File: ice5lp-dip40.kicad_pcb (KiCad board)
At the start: 4 copper layers, 17.8 x 50.8 mm, 44 parts, among them J1 Conn_02x04_Odd_Even, J2 Conn_01x20, J3 Conn_01x20, J4 USB_B_Micro, SW1 SW_Push, SW2 SW_Push, U1 AT25D011-SSHF, U2 MIC5355-S4YMME, U3 ICE5LP4K-SG48, X1 ECS-2520MV-500-BN-TR

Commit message: Archive project 3d models
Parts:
- C1, C10, C11, C12, C13, C15, C17, C18, C19, C2, C20, C3, C4, C7, C8, C9: footprint esynr3z_Capacitor:C_0603 -> lib_fp:C_0603
- D1: footprint esynr3z_Diode:SOD-523F -> lib_fp:SOD-523F
- D2: footprint esynr3z_LED:LED_Cree-PLCC4_2x2mm_CW -> lib_fp:LED_Cree-PLCC4_2x2mm_CW
- D3, D4, D5: footprint esynr3z_LED:LED_0603 -> lib_fp:LED_0603
- J1: footprint esynr3z_Connector:PinHeader_2x04_P2.54mm_Vertical -> lib_fp:PinHeader_2x04_P2.54mm_Vertical
- J2, J3: footprint esynr3z_Connector:PinHeader_1x20_P2.54mm_Vertical -> lib_fp:PinHeader_1x20_P2.54mm_Vertical
- J4: footprint esynr3z_ConnectorUSB:USB_Micro-B_Wurth_629105136821 -> lib_fp:USB_Micro-B_Wurth_629105136821
- R1, R10, R11, R12, R13, R2, R4, R5, R6, R7, R8, R9: footprint esynr3z_Resistor:R_0603 -> lib_fp:R_0603
- SW1, SW2: footprint esynr3z_Switch:PTS830 -> lib_fp:PTS830
- U1: footprint esynr3z_SO:SOIC-8_3.9x4.9mm_P1.27mm -> lib_fp:SOIC-8_3.9x4.9mm_P1.27mm
- U2: footprint esynr3z_SO:MSOP-8-1EP_3x3mm_P0.65mm_EP2.54x2.8mm_ThermalVias -> lib_fp:MSOP-8-1EP_3x3mm_P0.65mm_EP2.54x2.8mm_ThermalVias
- U3: footprint esynr3z_QFN:QFN-48-1EP_7x7mm_P0.5mm_EP5x5mm_ThermalVias -> lib_fp:QFN-48-1EP_7x7mm_P0.5mm_EP5x5mm_ThermalVias
- X1: footprint esynr3z_Oscillator:ECS-2520MV_4Pin_2.5x2.0mm -> lib_fp:ECS-2520MV_4Pin_2.5x2.0mm

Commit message: Replace 1Mb flash with 8Mb one
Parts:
- U1: value AT25D011-SSHF -> AT25D081-SSHD
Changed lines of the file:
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@@
     (uvia_drill 0.1)
+  )
+  (module lib_fp:SOIC-8_3.9x4.9mm_P1.27mm (layer B.Cu)
+    (at 195.58 71.247)
+    (descr "8-Lead Plastic Small Outline (SN) - Narrow, 3.90 mm Body [SOIC] (see Microchip Packaging Specification 00000049BS.pdf)")
+    (tags "soic 8")
+    (attr smd)
+    (fp_text reference U1 (at 0 3.5) (layer B.SilkS) hide
+      (effects (font (size 1 1) (thickness 0.15)) (justify mirror))
+    )
+    (fp_text value AT25D081-SSHD (at 0 -3.5) (layer B.Fab)
+      (effects (font (size 1 1) (thickness 0.15)) (justify mirror))
+    )
+    (fp_line (start -0.8 2.5) (end -1.6 1.7) (layer B.SilkS) (width 0.15))
+    (fp_line (start -1.6 -2.4) (end 1.6 -2.4) (layer B.SilkS) (width 0.15))
+    (fp_line (start -0.8 2.5) (end 1.6 2.5) (layer B.SilkS) (width 0.15))
+    (fp_line (start 1.6 2.5) (end 1.6 -2.4) (layer B.SilkS) (width 0.15))
+    (fp_line (start -1.6 -2.4) (end -1.6 1.7) (layer B.SilkS) (width 0.15))
+    (fp_line (start -3.73 -2.7) (end 3.73 -2.7) (layer B.CrtYd) (width 0.05))
+    (fp_line (start -3.73 2.7) (end 3.73 2.7) (layer B.CrtYd) (width 0.05))
+    (fp_line (start 3.73 2.7) (end 3.73 -2.7) (layer B.CrtYd) (width 0.05))
+    (fp_line (start -3.73 2.7) (end -3.73 -2.7) (layer B.CrtYd) (width 0.05))
+    (fp_line (start -1.95 1.45) (end -0.95 2.45) (layer B.Fab) (width 0.1))
+    (fp_line (start -1.95 -2.45) (end -1.95 1.45) (layer B.Fab) (width 0.1))
+    (fp_line (start 1.95 -2.45) (end -1.95 -2.45) (layer B.Fab) (width 0.1))
+    (fp_line (start 1.95 2.45) (end 1.95 -2.45) (layer B.Fab) (width 0.1))
+    (fp_line (start -0.95 2.45) (end 1.95 2.45) (layer B.Fab) (width 0.1))
+    (fp_text user %R (at 0 0) (layer B.Fab)
+      (effects (font (size 1 1) (thickness 0.15)) (justify mirror))
+    )
+    (pad 8 smd rect (at 2.7 1.905) (size 1.78 0.7) (layers B.Cu B.Paste B.Mask)
+      (net 53 VCC_IO))
+    (pad 7 smd rect (at 2.7 0.635) (size 1.78 0.7) (layers B.Cu B.Paste B.Mask)
+      (net 9 "Net-(R4-Pad2)"))
+    (pad 6 smd rect (at 2.7 -0.635) (size 1.78 0.7) (layers B.Cu B.Paste B.Mask)
+      (net 5 ICE_SCK))
+    (pad 5 smd rect (at 2.7 -1.905) (size 1.78 0.7) (layers B.Cu B.Paste B.Mask)
+      (net 7 FLASH_MOSI))
+    (pad 4 smd rect (at -2.7 -1.905) (size 1.78 0.7) (layers B.Cu B.Paste B.Mask)
+      (net 1 GND))
+    (pad 3 smd rect (at -2.7 -0.635) (size 1.78 0.7) (layers B.Cu B.Paste B.Mask)
+      (net 8 "Net-(R2-Pad2)"))
+    (pad 2 smd rect (at -2.7 0.635) (size 1.78 0.7) (layers B.Cu B.Paste B.Mask)
+      (net 4 FLASH_MISO))
+    (pad 1 smd rect (at -2.7 1.905) (size 1.78 0.7) (layers B.Cu B.Paste B.Mask)
+      (net 6 ICE_CSN))
+    (model ${KIPRJMOD}/3d_models/SOIC-8_3.9x4.9mm_P1.27mm.wrl
+      (at (xyz 0 0 0))
+      (scale (xyz 1 1 1))
+      (rotate (xyz 0 0 0))
+    )
   )
   (module esynr3z_Symbol:esynr3z_logo_4.5x8.4mm_Silk (layer B.Cu)
@@
     )
   )
-  (module lib_fp:SOIC-8_3.9x4.9mm_P1.27mm locked (layer B.Cu)
-    (at 195.58 71.247)
-    (descr "8-Lead Plastic Small Outline (SN) - Narrow, 3.90 mm Body [SOIC] (see Microchip Packaging Specification 00000049BS.pdf)")
-    (tags "SOIC 1.27")
-    (attr smd)
-    (fp_text reference U1 (at 0 3.5) (layer B.SilkS) hide
-      (effects (font (size 0.8 0.8) (thickness 0.15)) (justify mirror))
-    )
-    (fp_text value AT25D011-SSHF (at 0 -2.921) (layer B.Fab)
-      (effects (font (size 0.5 0.5) (thickness 0.125)) (justify mirror))
-    )
-    (fp_line (start -0.8 2.5) (end -1.6 1.7) (layer B.SilkS) (width 0.15))
-    (fp_line (start -1.6 -2.4) (end 1.6 -2.4) (layer B.SilkS) (width 0.15))
-    (fp_line (start -0.8 2.5) (end 1.6 2.5) (layer B.SilkS) (width 0.15))
-    (fp_line (start 1.6 2.5) (end 1.6 -2.4) (layer B.SilkS) (width 0.15))
-    (fp_line (start -1.6 -2.4) (end -1.6 1.7) (layer B.SilkS) (width 0.15))
-    (fp_line (start -3.73 -2.7) (end 3.73 -2.7) (layer B.CrtYd) (width 0.05))
-    (fp_line (start -3.73 2.7) (end 3.73 2.7) (layer B.CrtYd) (width 0.05))
-    (fp_line (start 3.73 2.7) (end 3.73 -2.7) (layer B.CrtYd) (width 0.05))
-    (fp_line (start -3.73 2.7) (end -3.73 -2.7) (layer B.CrtYd) (width 0.05))
-    (fp_line (start -1.95 1.45) (end -0.95 2.45) (layer B.Fab) (width 0.1))
-    (fp_line (start -1.95 -2.45) (end -1.95 1.45) (layer B.Fab) (width 0.1))
-    (fp_line (start 1.95 -2.45) (end -1.95 -2.45) (layer B.Fab) (width 0.1))
-    (fp_line (start 1.95 2.45) (end 1.95 -2.45) (layer B.Fab) (width 0.1))
-    (fp_line (start -0.95 2.45) (end 1.95 2.45) (layer B.Fab) (width 0.1))
-    (fp_text user %R (at 0 0) (layer B.Fab)
-      (effects (font (size 1 1) (thickness 0.15)) (justify mirror))
-    )
-    (pad 8 smd rect (at 2.7 1.905) (size 1.78 0.7) (layers B.Cu B.Paste B.Mask)
-      (net 53 VCC_IO))
-    (pad 7 smd rect (at 2.7 0.635) (size 1.78 0.7) (layers B.Cu B.Paste B.Mask)
-      (net 9 "Net-(R4-Pad2)"))
-    (pad 6 smd rect (at 2.7 -0.635) (size 1.78 0.7) (layers B.Cu B.Paste B.Mask)
-      (net 5 ICE_SCK))
-    (pad 5 smd rect (at 2.7 -1.905) (size 1.78 0.7) (layers B.Cu B.Paste B.Mask)
-      (net 7 FLASH_MOSI))
-    (pad 4 smd rect (at -2.7 -1.905) (size 1.78 0.7) (layers B.Cu B.Paste B.Mask)
-      (net 1 GND))
-    (pad 3 smd rect (at -2.7 -0.635) (size 1.78 0.7) (layers B.Cu B.Paste B.Mask)
-      (net 8 "Net-(R2-Pad2)"))
-    (pad 2 smd rect (at -2.7 0.635) (size 1.78 0.7) (layers B.Cu B.Paste B.Mask)
-      (net 4 FLASH_MISO))
-    (pad 1 smd rect (at -2.7 1.905) (size 1.78 0.7) (layers B.Cu B.Paste B.Mask)
-      (net 6 ICE_CSN))
-    (model ${KIPRJMOD}/3d_models/SOIC-8_3.9x4.9mm_P1.27mm.wrl
-      (at (xyz 0 0 0))
-      (scale (xyz 1 1 1))
-      (rotate (xyz 0 0 0))
-    )
-  )

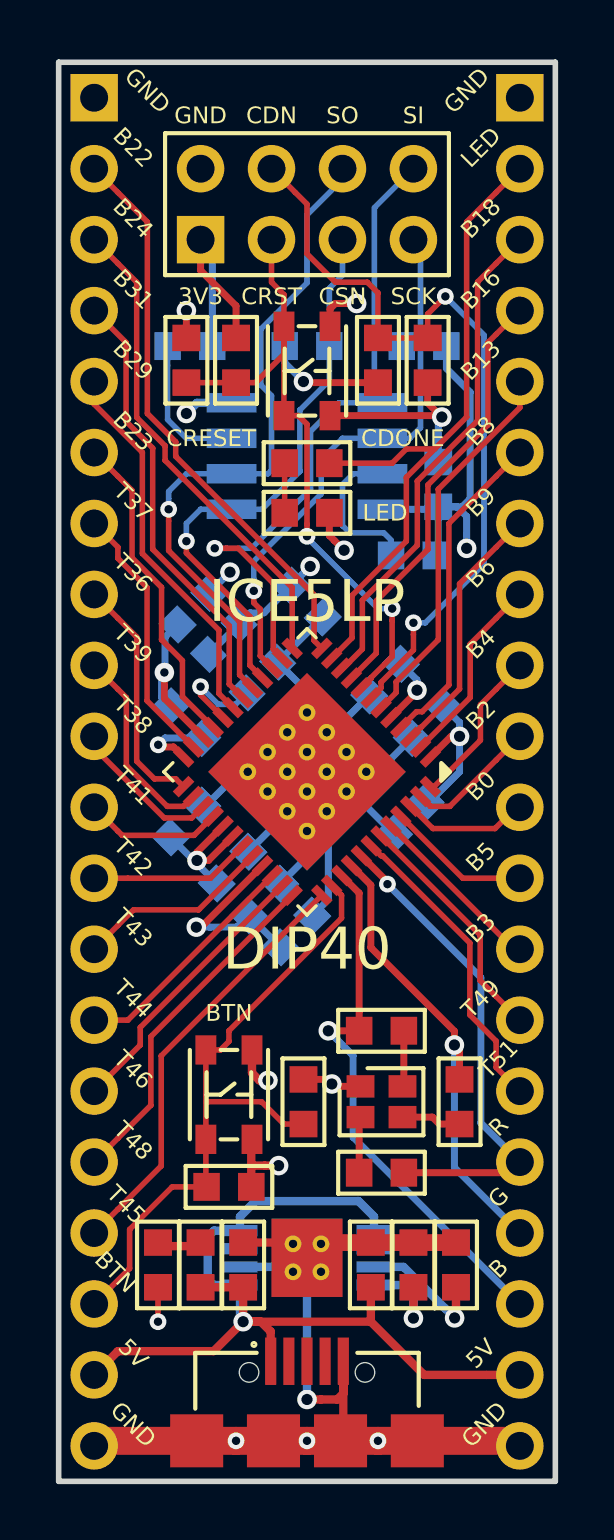
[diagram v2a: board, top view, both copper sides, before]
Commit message: Trace USB data lines into fpga
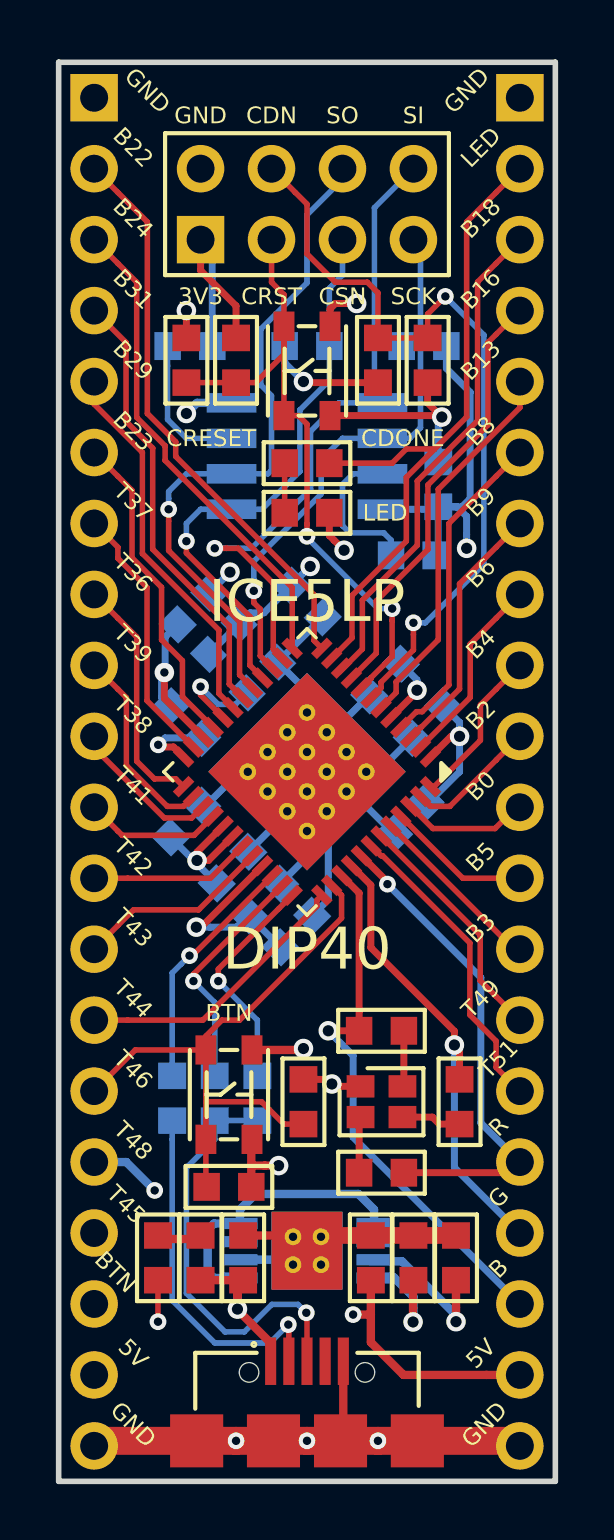
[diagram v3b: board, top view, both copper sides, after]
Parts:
- added R14: 68, lib_fp:R_0603, B.Cu at (192.3, 94.2)
- added R15: 68, lib_fp:R_0603, B.Cu at (190.8, 94.2)
- added R3: 1.5k, lib_fp:R_0603, B.Cu at (193.8, 94.2)
- moved G*** 1.91 mm to (199.0, 91.3)
- moved C20 0.25 mm to (193.3, 99.9)
- moved C3 0.25 mm to (197.9, 99.9)
- moved C7 0.25 mm to (199.4, 99.9)
- moved C8 0.25 mm to (200.9, 99.9)
- moved D4 0.25 mm to (190.2, 99.9)
- moved R11 0.25 mm to (191.8, 99.9)
- moved U2 0.25 mm to (195.6, 99.7)
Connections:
- J2 pad 14: IOT_44B -> IOT_45A
- J2 pad 15: IOT_46B -> ICE_BTN
- J2 pad 16: IOT_48B -> VCC_CORE
- J2 pad 17: IOT_45A -> VCC_IO
- J2 pad 18: ICE_BTN -> GND
- U3 pad 34: IOT_44B -> USB_N
- U3 pad 35: IOT_46B -> USB_P
- U3 pad 36: IOT_48B -> USB_PU
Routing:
- net Net-(J4-Pad3): track 0.00 -> 15.3 mm, vias 0 -> 1
- net Net-(J4-Pad2): track 0.00 -> 12.8 mm, vias 0 -> 1
- net IOT_48B: track 12.5 -> 0.00 mm
- net IOT_46B: track 10.2 -> 0.00 mm
- net VCC_CORE: track 46.2 -> 55.9 mm, vias 3 -> 4
- net USB_N: track 0.00 -> 8.72 mm, vias 0 -> 1
- net IOT_44B: track 8.53 -> 0.00 mm
- net USB_P: track 0.00 -> 8.45 mm, vias 0 -> 1
- net USB_PU: track 0.00 -> 8.14 mm, vias 0 -> 1
- net GND: track 89.7 -> 82.5 mm, vias 13 -> 12
- net IOT_45A: track 15.5 -> 10.1 mm
- net VCC_IO: track 179.2 -> 182.8 mm
- net ICE_BTN: track 23.7 -> 21.8 mm
- net +5V: track 34.5 -> 36.2 mm, vias 1 -> 2

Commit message: Update docs and generator info
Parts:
- X1: value ECS-2520MV-500-BN-TR -> ECS-2520MV-120-BN-TR
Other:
- board text added: "ice5lp-dip40 rev.A"
- board text removed: "ice5lp-dip40 v1.0"
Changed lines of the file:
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@@
   )
   (page A4)
+  (title_block
+    (title "Lattice iCE5LP4K DIP40 breakout board")
+    (rev A)
+  )
   (layers
     (0 F.Cu signal)
-    (1 In1.VCC.Cu power)
-    (2 In2.GND.Cu power)
+    (1 In1.VCC.Cu power hide)
+    (2 In2.GND.Cu power hide)
     (31 B.Cu mixed)
     (36 B.SilkS user)
-    (37 F.SilkS user hide)
+    (37 F.SilkS user)
     (38 B.Mask user hide)
     (39 F.Mask user hide)
@@
       (effects (font (size 0.8 0.8) (thickness 0.15)) (justify mirror))
     )
-    (fp_text value ECS-2520MV-500-BN-TR (at 0 -1.436841 315) (layer B.Fab)
+    (fp_text value ECS-2520MV-120-BN-TR (at 0 -1.436841 315) (layer B.Fab)
       (effects (font (size 0.5 0.5) (thickness 0.125)) (justify mirror))
     )
@@
     )
   )
-  (gr_text "ice5lp-dip40 v1.0" (at 195.58 58.547) (layer B.SilkS)
+  (gr_text "ice5lp-dip40 rev.A" (at 195.58 58.547) (layer B.SilkS)
     (effects (font (size 0.8 0.8) (thickness 0.15)) (justify mirror))
   )

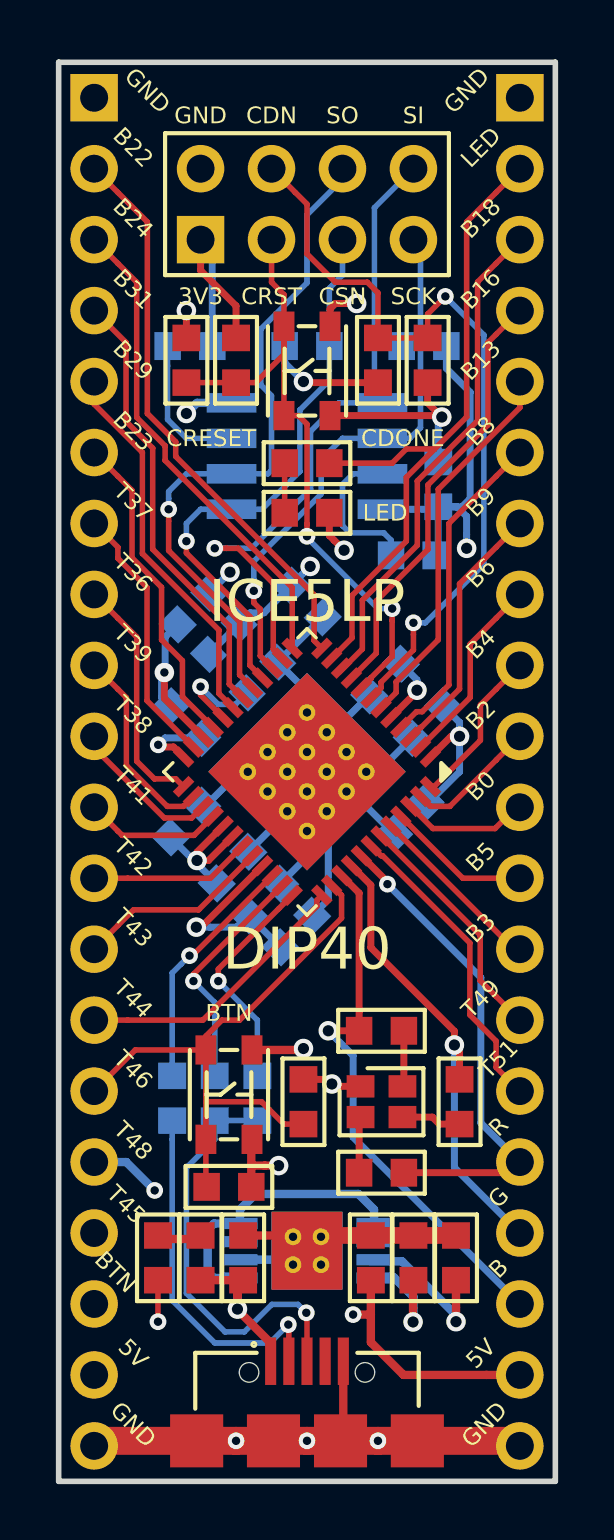
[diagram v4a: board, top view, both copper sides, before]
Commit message: Add info about other fpga supported
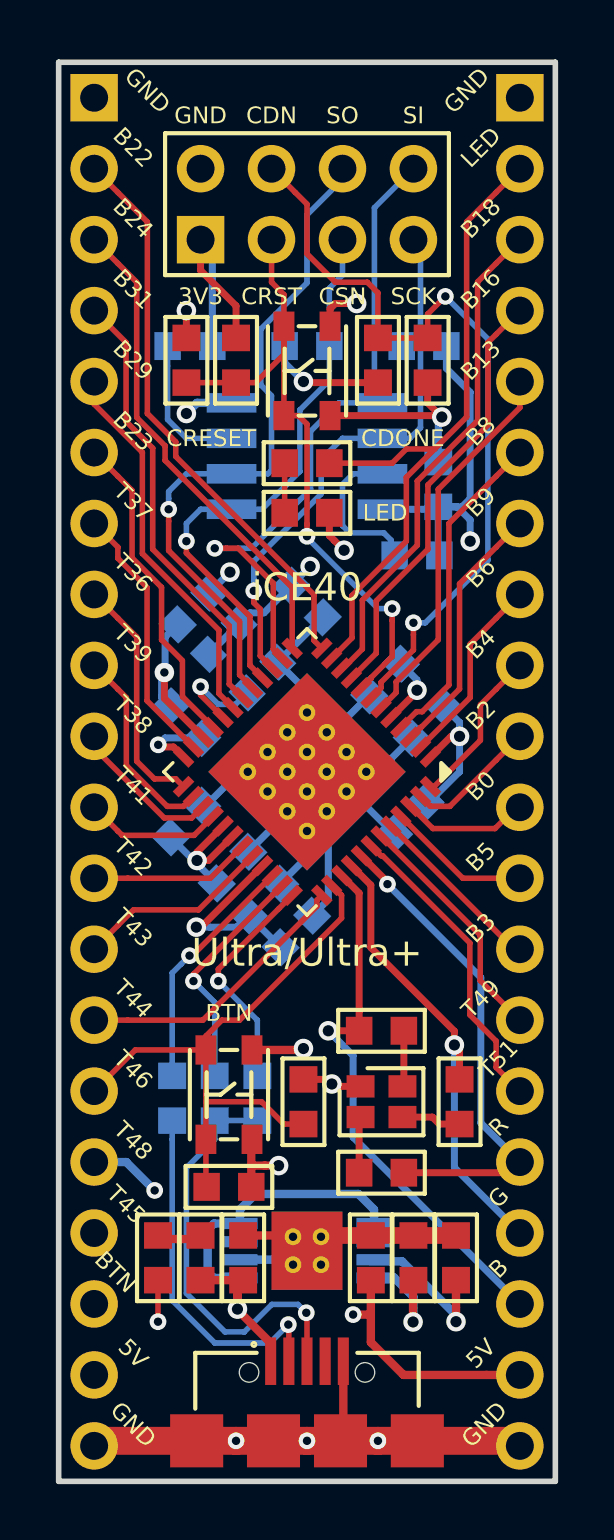
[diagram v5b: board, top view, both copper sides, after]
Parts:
- moved R4 0.13 mm to (199.5, 74.8)
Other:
- board text added: "Ultra/Ultra+"
- board text added: "iCE40"
- board text added: "ice40-dip40"
- board text added: "rev.A"
- board text removed: "DIP40"
- board text removed: "ICE5LP"
- board text removed: "ice5lp-dip40 rev.A"
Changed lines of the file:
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@@
   (general
     (thickness 1.6)
-    (drawings 62)
-    (tracks 661)
+    (drawings 63)
+    (tracks 660)
     (zones 0)
     (modules 47)
@@
     (31 B.Cu mixed)
     (36 B.SilkS user)
-    (37 F.SilkS user)
+    (37 F.SilkS user hide)
     (38 B.Mask user hide)
     (39 F.Mask user hide)
@@
     (44 Edge.Cuts user)
     (45 Margin user)
-    (46 B.CrtYd user)
-    (47 F.CrtYd user hide)
+    (46 B.CrtYd user hide)
+    (47 F.CrtYd user)
     (48 B.Fab user hide)
-    (49 F.Fab user hide)
+    (49 F.Fab user)
   )
   (setup
@@
   )
   (module lib_fp:R_0603 locked (layer B.Cu)
-    (at 199.39 74.803 180)
+    (at 199.517 74.803 180)
     (descr "SMD 0603 (1608 Metric)")
     (tags "resistor 0603")
@@
     )
   )
-  (gr_text "ice5lp-dip40 rev.A" (at 195.58 58.547) (layer B.SilkS)
+  (gr_text rev.A (at 195.58 105.029) (layer B.SilkS)
+    (effects (font (size 0.8 0.8) (thickness 0.15)) (justify mirror))
+  )
+  (gr_text ice40-dip40 (at 195.58 58.547) (layer B.SilkS)
     (effects (font (size 0.8 0.8) (thickness 0.15)) (justify mirror))
   )
@@
     (effects (font (size 1 1) (thickness 0.18)) (justify mirror))
   )
-  (gr_text DIP40 (at 195.58 88.9) (layer F.SilkS)
-    (effects (font (size 1.5 1.5) (thickness 0.3)))
+  (gr_text Ultra/Ultra+ (at 195.58 89.027) (layer F.SilkS)
+    (effects (font (size 1 1) (thickness 0.25)))
   )
-  (gr_text ICE5LP (at 195.58 76.454) (layer F.SilkS)
-    (effects (font (size 1.5 1.5) (thickness 0.3)))
+  (gr_text iCE40 (at 195.58 75.946) (layer F.SilkS)
+    (effects (font (size 1 1) (thickness 0.25)))
   )
   (gr_text BTN (at 192.786 91.186) (layer F.SilkS)
@@
   (segment (start 199.39 78.188122) (end 199.39 77.640264) (width 0.2) (layer F.Cu) (net 2))
   (segment (start 197.878097 79.89835) (end 198.23165 79.544797) (width 0.2) (layer F.Cu) (net 2))
-  (segment (start 200.533 65.532) (end 201.915002 66.914002) (width 0.2) (layer B.Cu) (net 2))
   (segment (start 199.814264 77.216) (end 199.39 77.216) (width 0.2) (layer B.Cu) (net 2))
-  (segment (start 201.915002 66.914002) (end 201.915002 75.115262) (width 0.2) (layer B.Cu) (net 2))
-  (segment (start 201.915002 75.115262) (end 199.814264 77.216) (width 0.2) (layer B.Cu) (net 2))
+  (segment (start 202.057 74.973264) (end 199.814264 77.216) (width 0.2) (layer B.Cu) (net 2))
+  (segment (start 200.533 65.532) (end 202.057 67.056) (width 0.2) (layer B.Cu) (net 2))
+  (segment (start 202.057 67.056) (end 202.057 74.973264) (width 0.2) (layer B.Cu) (net 2))
   (segment (start 191.262 68.618) (end 193.04 68.618) (width 0.2) (layer F.Cu) (net 3) (status 30))
   (segment (start 194.755 67.324) (end 194.755 66.599) (width 0.2) (layer F.Cu) (net 3) (status 20))
@@
   (segment (start 195.453 68.58) (end 195.103001 68.929999) (width 0.6) (layer In1.VCC.Cu) (net 50))
   (segment (start 195.103001 68.929999) (end 193.579001 68.929999) (width 0.6) (layer In1.VCC.Cu) (net 50))
-  (via (at 201.295 74.549004) (size 0.7) (drill 0.4) (layers F.Cu B.Cu) (net 50))
   (segment (start 201.295 81.534001) (end 201.295 75.043978) (width 0.6) (layer In1.VCC.Cu) (net 50))
   (segment (start 201.295 75.043978) (end 201.295 74.549004) (width 0.6) (layer In1.VCC.Cu) (net 50))
@@
   (segment (start 193.490315 87.687685) (end 193.066477 88.111523) (width 0.25) (layer B.Cu) (net 50))
   (segment (start 191.786244 88.111523) (end 191.616523 88.111523) (width 0.25) (layer F.Cu) (net 50))
-  (segment (start 201.295 73.406) (end 201.295 74.05403) (width 0.25) (layer B.Cu) (net 50))
-  (segment (start 200.279 73.063) (end 200.952 73.063) (width 0.25) (layer B.Cu) (net 50))
-  (segment (start 201.295 74.05403) (end 201.295 74.549004) (width 0.25) (layer B.Cu) (net 50))
-  (segment (start 200.952 73.063) (end 201.295 73.406) (width 0.25) (layer B.Cu) (net 50))
   (segment (start 198.6915 100.6475) (end 199.39 101.346) (width 0.3) (layer B.Cu) (net 50))
   (segment (start 199.39 101.346) (end 199.39 102.108) (width 0.3) (layer B.Cu) (net 50))
@@
   (segment (start 189.357 84.944696) (end 189.592696 84.709) (width 0.6) (layer In1.VCC.Cu) (net 50))
   (segment (start 189.357 99.06) (end 189.357 84.944696) (width 0.6) (layer In1.VCC.Cu) (net 50))
+  (segment (start 201.422 73.533) (end 201.422 74.422004) (width 0.25) (layer B.Cu) (net 50))
+  (segment (start 200.279 73.063) (end 200.952 73.063) (width 0.25) (layer B.Cu) (net 50))
+  (segment (start 200.952 73.063) (end 201.422 73.533) (width 0.25) (layer B.Cu) (net 50))
+  (via (at 201.422 74.295) (size 0.7) (drill 0.4) (layers F.Cu B.Cu) (net 50))
   (segment (start 195.58 103.65) (end 195.58 101.940658) (width 0.2) (layer F.Cu) (net 52))
   (segment (start 195.58 101.940658) (end 195.554826 101.915484) (width 0.2) (layer F.Cu) (net 52))
